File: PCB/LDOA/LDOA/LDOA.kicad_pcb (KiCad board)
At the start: 2 copper layers, 20 parts, among them Q1 BC547, Q2 BC547, Q3 BC557, Q4 BC547, Q5 BC557, Q6 BC547, Q7 2N7000, Q8 IRF9520

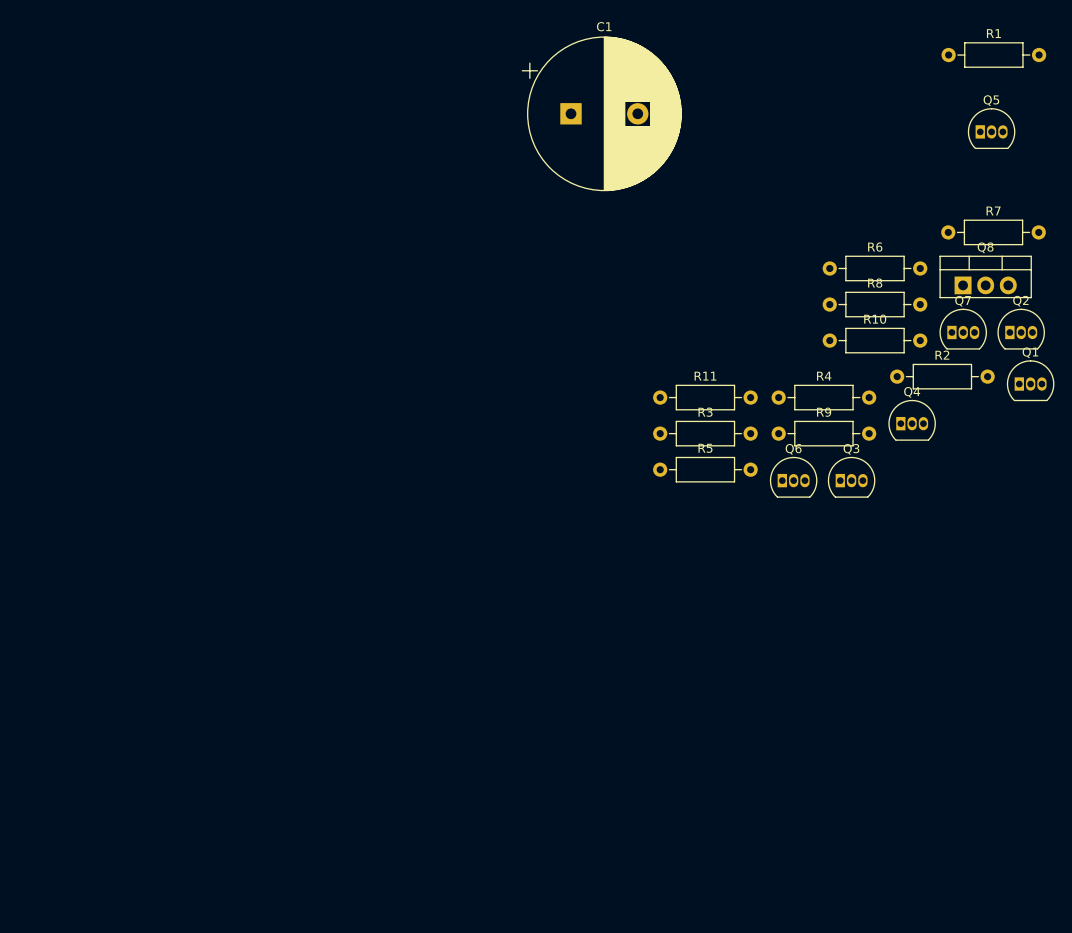
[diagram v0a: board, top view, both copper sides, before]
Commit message: Se acomodaron componentes en el PCB del circuito LDOA, También se agregó el foldback. Todavía falta sumar el UVLO OVLO, y poner los bornes para entradas y salidas del circuito.
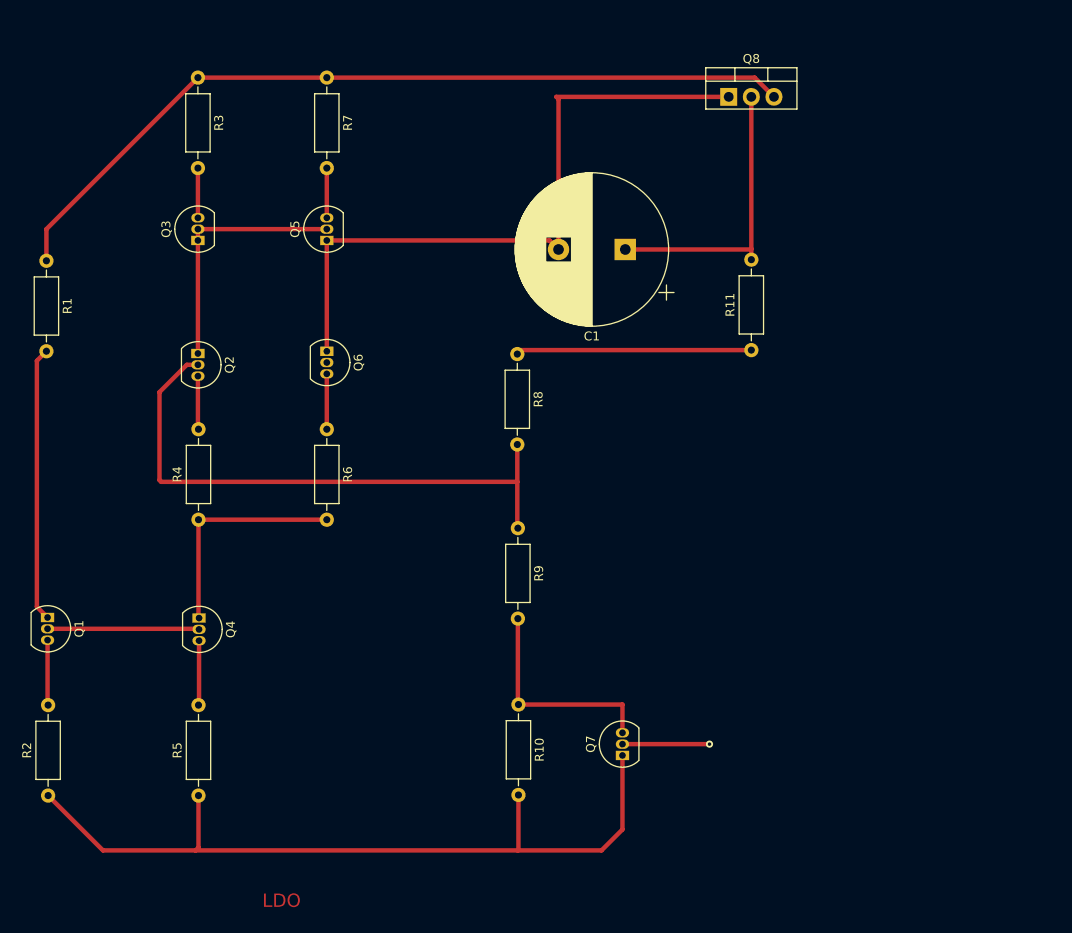
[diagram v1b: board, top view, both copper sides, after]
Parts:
- moved Q1 112.3 mm to (52.5, 102.8), turned to 270 degrees
- moved R2 106.4 mm to (52.5, 122.8), turned to 90 degrees
- moved R1 103.9 mm to (52.3, 62.7), turned to 270 degrees
- moved Q2 91.2 mm to (69.3, 73.2), turned to 270 degrees
- moved Q4 81.8 mm to (69.5, 102.9), turned to 270 degrees
- moved Q3 77.0 mm to (69.3, 60.5), turned to 90 degrees
- moved Q5 74.4 mm to (83.8, 60.5), turned to 90 degrees
- moved R7 71.9 mm to (83.8, 42.2), turned to 270 degrees
- moved R4 66.6 mm to (69.4, 91.8), turned to 90 degrees
- moved R3 65.5 mm to (69.3, 42.2), turned to 270 degrees
- moved R5 63.5 mm to (69.4, 122.8), turned to 90 degrees
- moved Q7 60.2 mm to (117.0, 118.3), turned to 90 degrees
- moved R6 59.3 mm to (83.8, 81.7), turned to 270 degrees
- moved R10 53.8 mm to (105.3, 112.6), turned to 270 degrees
- moved Q6 53.2 mm to (83.8, 72.9), turned to 270 degrees
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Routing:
- net Net-(Q8-Pad3): track 0.00 -> 93.2 mm
- net Net-(Q7-Pad1): track 0.00 -> 88.9 mm
- net Net-(C1-Pad2): track 0.00 -> 75.5 mm
- net Vf: track 0.00 -> 65.2 mm
- net Net-(Q1-Pad1): track 0.00 -> 47.9 mm
- net Net-(C1-Pad1): track 0.00 -> 32.5 mm
- net Net-(Q2-Pad1): track 0.00 -> 28.4 mm
- net VA: track 0.00 -> 26.5 mm
- net Net-(Q4-Pad1): track 0.00 -> 25.5 mm
- net Net-(Q7-Pad3): track 0.00 -> 24.5 mm
- net SELA: track 0.00 -> 9.78 mm, vias 0 -> 1
- net Net-(Q1-Pad3): track 0.00 -> 7.33 mm
- net Net-(Q4-Pad3): track 0.00 -> 7.27 mm
- net Net-(Q6-Pad3): track 0.00 -> 6.22 mm
- net Net-(Q2-Pad3): track 0.00 -> 6.00 mm
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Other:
- board text added: "LDO"

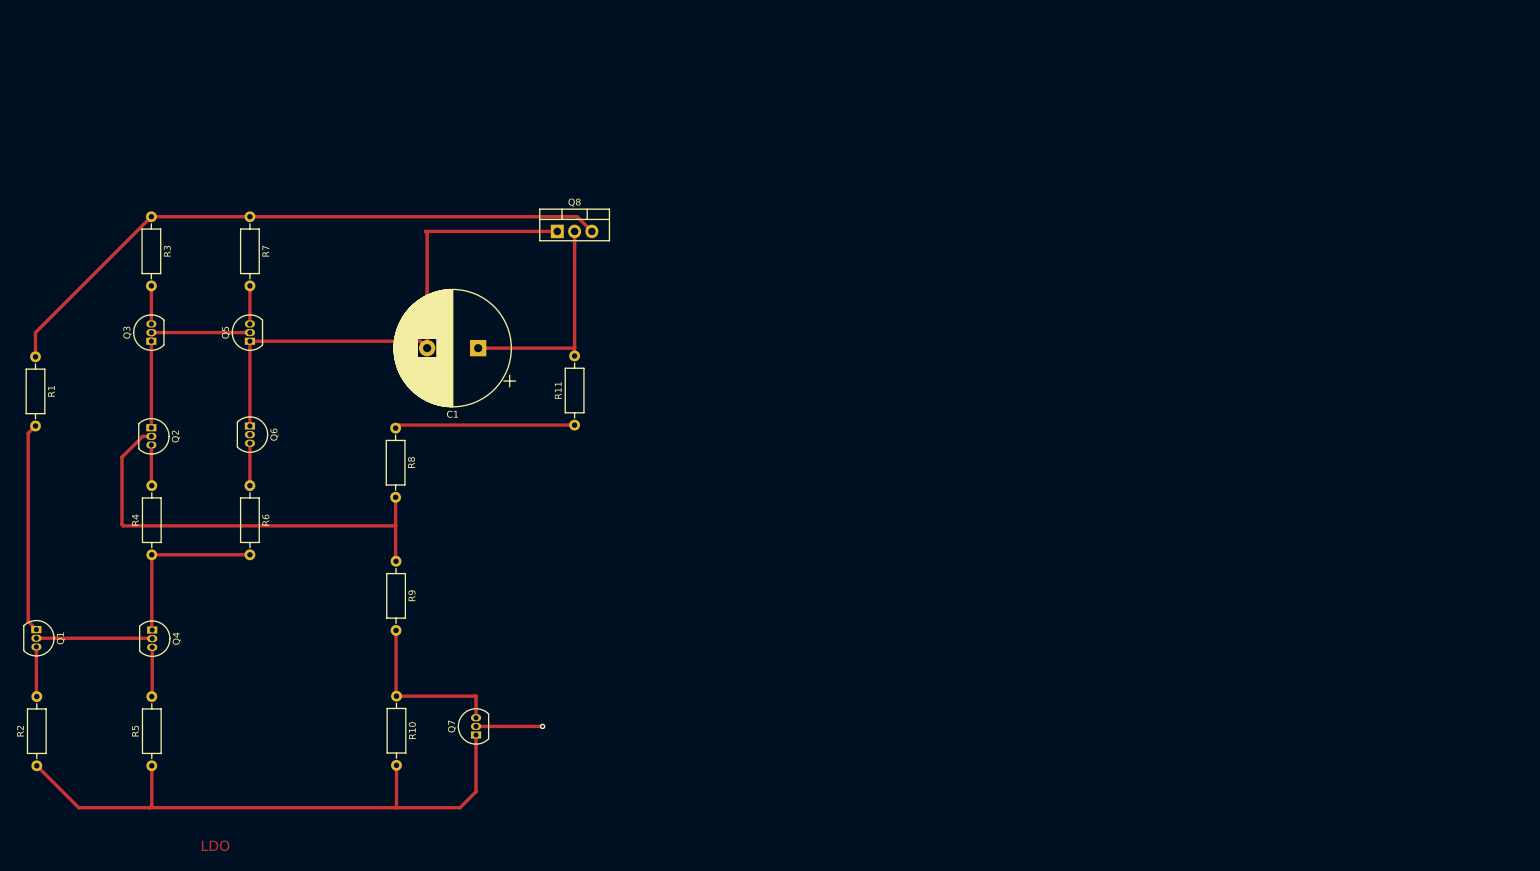
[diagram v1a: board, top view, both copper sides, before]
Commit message: Se agregaron más componentes al PCB. Hay que seguir trabajando con la distrubicion de los componentes
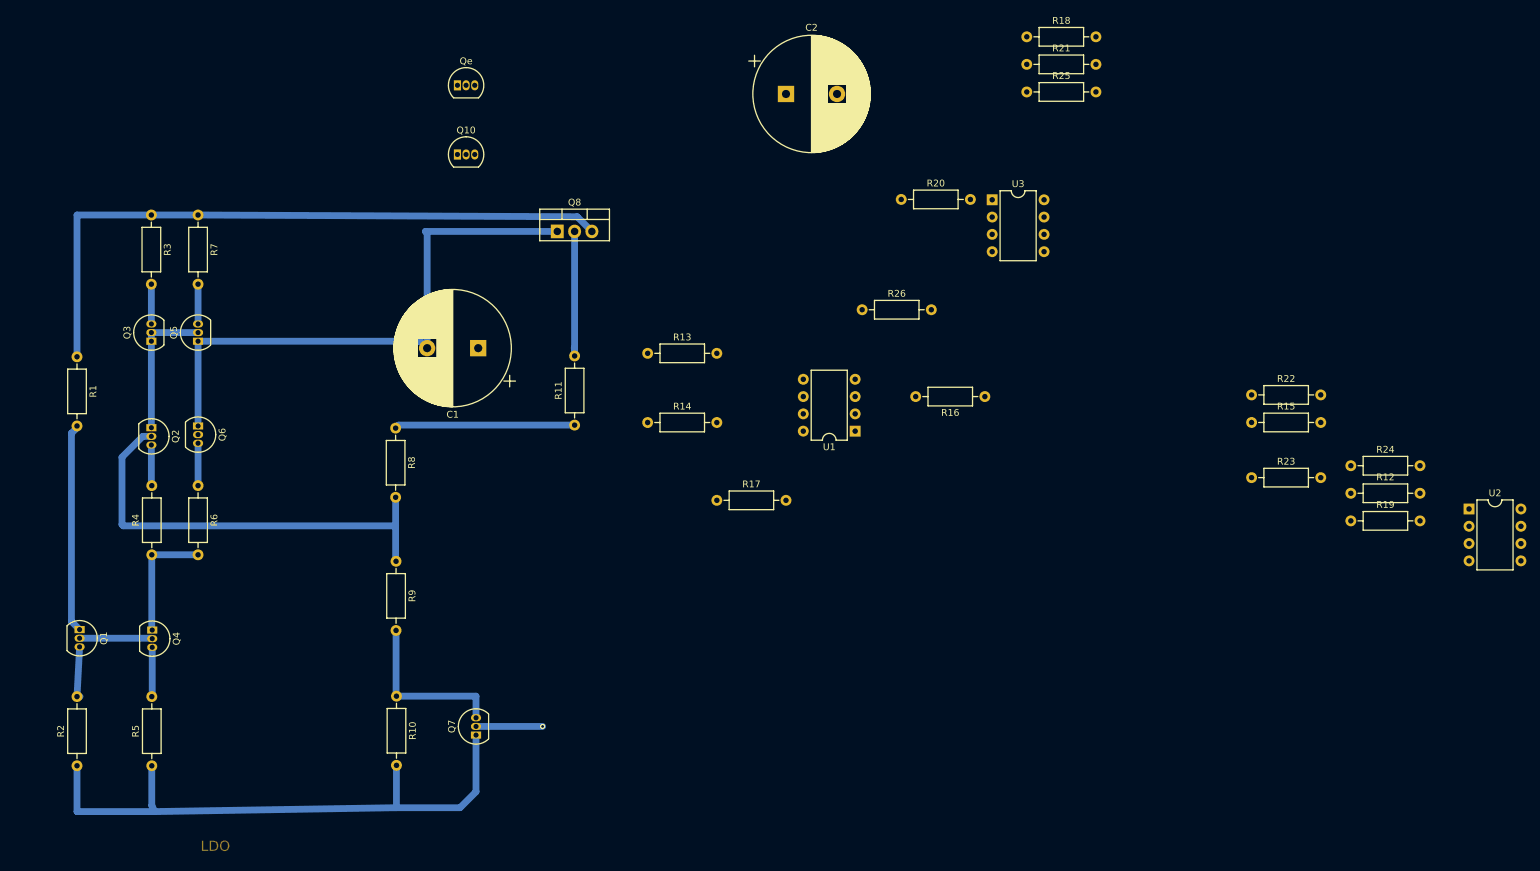
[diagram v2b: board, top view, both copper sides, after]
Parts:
- added C2: C, Capacitor_THT:CP_Radial_D17.0mm_P7.50mm, F.Cu at (162.6, 24.1)
- added Q10: BS250, Package_TO_SOT_THT:TO-92_Inline, F.Cu at (114.3, 33.0)
- added Qe: BS250, Package_TO_SOT_THT:TO-92_Inline, F.Cu at (114.3, 22.9)
- added R12: R, Resistor_THT:R_Axial_DIN0207_L6.3mm_D2.5mm_P10.16mm_Horizontal, F.Cu at (245.5, 82.8)
- added R13: R, Resistor_THT:R_Axial_DIN0207_L6.3mm_D2.5mm_P10.16mm_Horizontal, F.Cu at (142.2, 62.2)
- added R14: R, Resistor_THT:R_Axial_DIN0207_L6.3mm_D2.5mm_P10.16mm_Horizontal, F.Cu at (142.2, 72.4)
- added R15: R, Resistor_THT:R_Axial_DIN0207_L6.3mm_D2.5mm_P10.16mm_Horizontal, F.Cu at (230.9, 72.4)
- added R16: R, Resistor_THT:R_Axial_DIN0207_L6.3mm_D2.5mm_P10.16mm_Horizontal, F.Cu at (191.8, 68.6)
- added R17: R, Resistor_THT:R_Axial_DIN0207_L6.3mm_D2.5mm_P10.16mm_Horizontal, F.Cu at (152.4, 83.8)
- added R18: R, Resistor_THT:R_Axial_DIN0207_L6.3mm_D2.5mm_P10.16mm_Horizontal, F.Cu at (197.9, 15.7)
- added R19: R, Resistor_THT:R_Axial_DIN0207_L6.3mm_D2.5mm_P10.16mm_Horizontal, F.Cu at (245.5, 86.8)
- added R20: R, Resistor_THT:R_Axial_DIN0207_L6.3mm_D2.5mm_P10.16mm_Horizontal, F.Cu at (179.5, 39.6)
- added R21: R, Resistor_THT:R_Axial_DIN0207_L6.3mm_D2.5mm_P10.16mm_Horizontal, F.Cu at (197.9, 19.8)
- added R22: R, Resistor_THT:R_Axial_DIN0207_L6.3mm_D2.5mm_P10.16mm_Horizontal, F.Cu at (230.9, 68.3)
- added R23: R, Resistor_THT:R_Axial_DIN0207_L6.3mm_D2.5mm_P10.16mm_Horizontal, F.Cu at (230.9, 80.5)
- added R24: R, Resistor_THT:R_Axial_DIN0207_L6.3mm_D2.5mm_P10.16mm_Horizontal, F.Cu at (245.5, 78.7)
- added R25: R, Resistor_THT:R_Axial_DIN0207_L6.3mm_D2.5mm_P10.16mm_Horizontal, F.Cu at (197.9, 23.8)
- added R26: R, Resistor_THT:R_Axial_DIN0207_L6.3mm_D2.5mm_P10.16mm_Horizontal, F.Cu at (173.7, 55.8)
- added U1: TL081, Package_DIP:DIP-8_W7.62mm, F.Cu at (172.7, 73.7)
- added U2: TL081, Package_DIP:DIP-8_W7.62mm, F.Cu at (262.9, 85.1)
- added U3: TL081, Package_DIP:DIP-8_W7.62mm, F.Cu at (192.8, 39.7)
- moved R7 7.62 mm to (76.2, 41.9)
- moved Q5 7.62 mm to (76.2, 60.5)
- moved Q6 7.62 mm to (76.2, 72.9)
- moved R6 7.62 mm to (76.2, 81.7)
- moved Q1 6.35 mm to (58.8, 102.8)
- moved R1 6.10 mm to (58.4, 62.7)
- moved R2 5.91 mm to (58.4, 122.8)
- moved R3 0.25 mm to (69.3, 41.9)
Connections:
- net Net-(Q7-Pad1) renamed GND
- net Net-(Q8-Pad3) renamed VREG
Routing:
- net Net-(C1-Pad1): track 32.5 -> 18.4 mm
- net Net-(Q4-Pad1): track 25.5 -> 17.9 mm
- net Net-(Q2-Pad1): track 28.4 -> 20.8 mm
- net Net-(C1-Pad2): track 75.5 -> 83.1 mm
- net Net-(Q1-Pad1): track 47.9 -> 41.5 mm
- net VREG: track 93.2 -> 97.5 mm
- net GND: track 88.9 -> 87.7 mm

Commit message: Se agregaron mas pistas. Hay que avanzar con la inclusion del UVLO OVLO, terminales y demás
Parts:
- C1: footprint Capacitor_THT:CP_Radial_D17.0mm_P7.50mm -> Capacitor_THT:C_Disc_D5.0mm_W2.5mm_P5.00mm
- C2: footprint Capacitor_THT:CP_Radial_D17.0mm_P7.50mm -> Capacitor_THT:C_Disc_D4.7mm_W2.5mm_P5.00mm
- moved R12 149.3 mm to (96.5, 73.7), turned to 180 degrees
- moved R15 136.8 mm to (96.5, 97.8), turned to 270 degrees
- moved R19 116.5 mm to (129.5, 97.8), turned to 90 degrees
- moved R18 115.2 mm to (163.8, 125.7), turned to 90 degrees
- moved U2 112.6 mm to (152.4, 106.7), turned to 180 degrees
- moved R23 95.2 mm to (143.5, 118.1)
- moved R21 93.3 mm to (163.8, 106.7), turned to 90 degrees
- moved R20 81.0 mm to (114.3, 87.6)
- moved R22 74.6 mm to (158.8, 49.5)
- moved C2 53.9 mm to (199.4, 63.5), turned to 90 degrees
- moved R24 47.4 mm to (200.7, 94.0), turned to 180 degrees
- moved U3 42.1 mm to (199.4, 81.3), turned to 180 degrees
- moved Q10 39.9 mm to (146.1, 57.1)
- moved Q9 39.9 mm to (146.1, 47.0)
- moved R16 27.4 mm to (181.6, 94.0), turned to 90 degrees
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- renumbered Qe to Q9
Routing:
- net VREG: track 97.5 -> 242.7 mm
- net GND: track 87.7 -> 218.8 mm
- net /V-: track 0.00 -> 91.2 mm
- net Net-(R23-Pad2): track 0.00 -> 76.0 mm
- net /Vact: track 0.00 -> 73.0 mm
- net Net-(R22-Pad2): track 0.00 -> 55.8 mm
- net /Vsens: track 0.00 -> 50.8 mm
- net Net-(R14-Pad2): track 0.00 -> 48.7 mm
- net Net-(R13-Pad2): track 0.00 -> 44.0 mm
- net /Vref2: track 0.00 -> 38.9 mm
- net Net-(R19-Pad2): track 0.00 -> 33.7 mm
- net Net-(R12-Pad1): track 0.00 -> 33.0 mm
- net Net-(C1-Pad2): track 83.1 -> 115.9 mm
- net Net-(C1-Pad1): track 18.4 -> 40.1 mm
- net Net-(R18-Pad2): track 0.00 -> 21.4 mm
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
